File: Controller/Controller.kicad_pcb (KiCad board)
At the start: 2 copper layers, 151.1 x 80 mm, 66 parts, among them IC1 LMP7715MF, J1 Probes, J10 Chlorine Level, J11 EXT_2, J12 Temp2, J13 J1B1211CCD, J14 Acid Pump, J15 Chlorine Pump, J16 Filtration Pump, J17 Lighting, J18 Relay_Ext, J19 Flood sensor, J2 Display, J20 EXT_I2C, J21 EXT_UART, J22 1775485-2, J3 ESP32, J4 EXT_SPI, J5 EXT_1, J6 Pressure, J7 Acid Level, J8 VInput, J9 Temp1, K1 ALQ305, K2 ALQ305, K3 ALQ305, K4 ALQ305, K5 ALQ305, U1 Teensy4.1, U3 V7805-1000, U4 V7803-1000, U5 ULN2003A

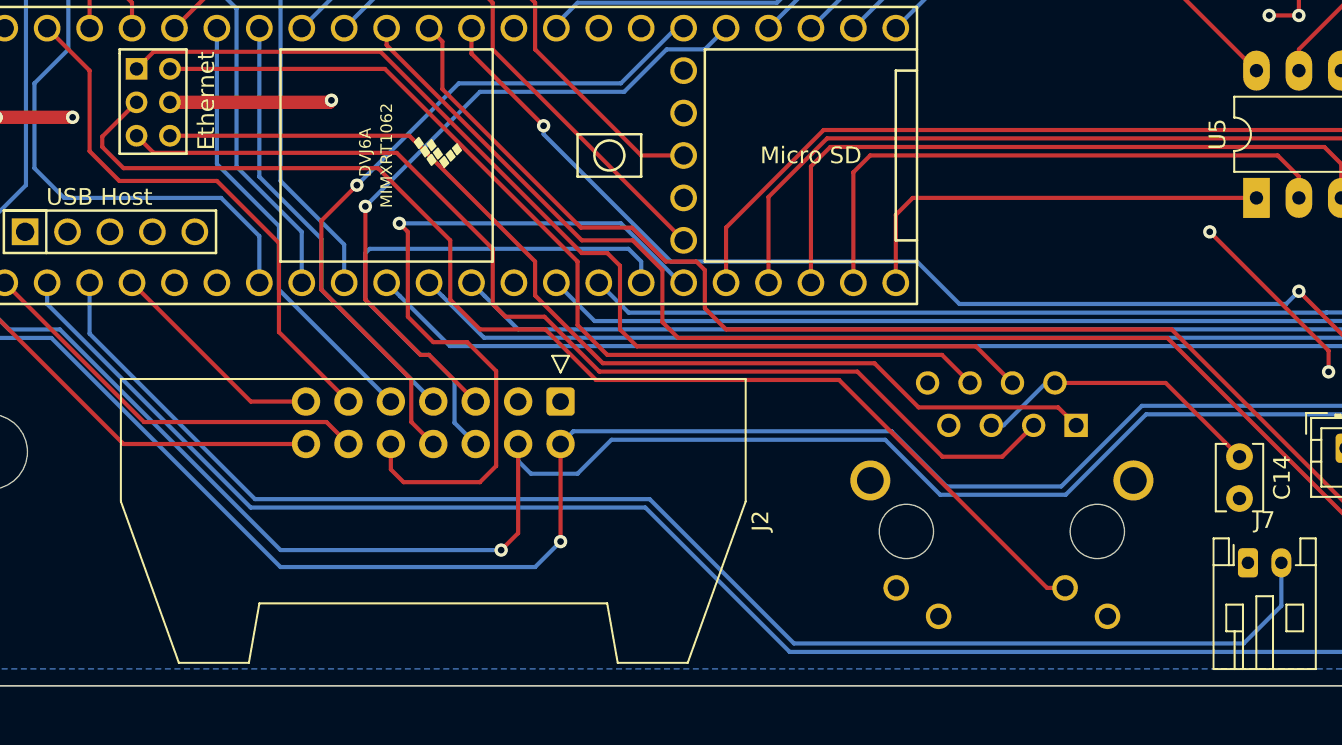
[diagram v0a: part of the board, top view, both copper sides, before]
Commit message: Ethernet on front
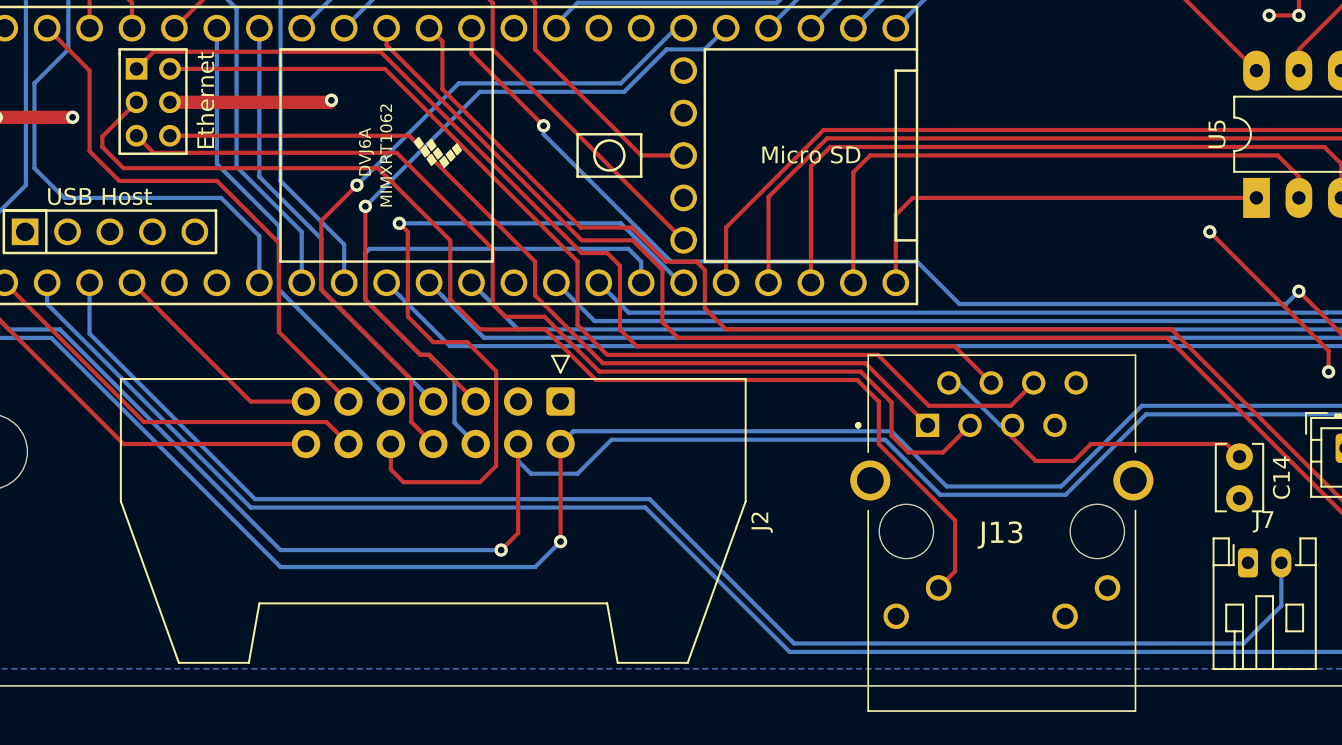
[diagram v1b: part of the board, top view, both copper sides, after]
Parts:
- J13: moved to F.Cu
- turned J13 to 0 degrees
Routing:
- net ETH_TX+: track 62.6 -> 53.7 mm
- net ETH_RX-: track 57.9 -> 62.9 mm
- net ETH_TX-: track 64.4 -> 61.5 mm
- net Net-(C14-Pad1): track 17.7 -> 20.5 mm
- net ETH_LED: track 74.2 -> 71.9 mm
- net ETH_RX+: track 63.3 -> 62.0 mm
